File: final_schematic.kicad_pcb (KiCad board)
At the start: 2 copper layers, 47 parts, among them J1 Battery Babysitter, J2 BB_SYSOFF, J3 BOOT0, J4 OLED Qwiic, J5 Programmer, J8 GPS_COAX, SW1 SW_Push_SESS, SW2 SW_Push_RADIO, SW3 SW_Push_RST, U1 STM32L476VGTx, U2 MTK3339, U3 RFM95W-868S2, U4 BNO055, U5 LT1129-3.3_SO8

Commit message: pcb checkpoint
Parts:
- added REF**: MountingHole_2.1mm, MountingHole:MountingHole_2.1mm, F.Cu at (144.4, 67.7)
- added REF**: MountingHole_2.1mm, MountingHole:MountingHole_2.1mm, F.Cu at (116.5, 67.7)
- C10, C11, C14, C15, C16, C17, C2, C3, C4, C5, C6, C7, C8, C9: moved to B.Cu
- moved C8 97.0 mm to (138.0, 88.9), turned to 270 degrees
- moved C6 94.2 mm to (137.5, 79.7), turned to 270 degrees
- moved C10 87.6 mm to (134.8, 90.1), turned to 180 degrees
- moved R1 86.6 mm to (121.8, 68.0)
- moved C11 85.4 mm to (129.6, 90.1)
- moved D1 84.5 mm to (121.8, 64.3)
- moved C9 84.4 mm to (126.4, 88.5), turned to 90 degrees
- moved J3 75.6 mm to (116.8, 86.7), turned to 270 degrees
- moved R6 73.6 mm to (115.9, 89.1), turned to 180 degrees
- moved C4 72.8 mm to (115.0, 91.9), turned to 90 degrees
- moved C5 71.9 mm to (118.8, 91.3), turned to 90 degrees
- moved C7 60.9 mm to (127.5, 78.5)
- moved J5 55.3 mm to (120.5, 72.2), turned to 0 degrees
- moved U5 30.1 mm to (128.0, 106.0), turned to 270 degrees
- moved C12 29.5 mm to (126.1, 98.6), turned to 180 degrees
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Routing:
- net GND: track 0.00 -> 200.4 mm
- net 3V3: track 0.00 -> 127.2 mm, vias 0 -> 1
- net I2C1_SCL: track 0.00 -> 15.8 mm
- net I2C1_SDA: track 0.00 -> 14.6 mm
- net USART_TX: track 0.00 -> 12.6 mm
- net BOOT0: track 0.00 -> 10.7 mm
- net SWDIO: track 0.00 -> 9.47 mm
- net Net-(C2-Pad2): track 0.00 -> 7.06 mm
- net V_supply: track 0.00 -> 6.94 mm
- net Net-(C3-Pad2): track 0.00 -> 6.82 mm
- net SWCLK: track 0.00 -> 5.13 mm
- net Net-(LoRa_CON_Coaxial1-Pad1): track 0.00 -> 4.23 mm
- net Net-(J8-Pad1): track 0.00 -> 3.76 mm
- net IMU_nRST: track 0.00 -> 3.04 mm
- net DIO0: track 0.00 -> 2.85 mm
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
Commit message: PCB deconstruction
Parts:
- added REF**: MountingHole_2.1mm, MountingHole:MountingHole_2.1mm, F.Cu at (143.2, 97.8)
- added REF**: MountingHole_2.1mm, MountingHole:MountingHole_2.1mm, F.Cu at (116.6, 97.8)
- moved D1 3.41 mm to (120.2, 61.3)
- moved R1 3.41 mm to (120.2, 65.0)
- moved REF** 1.27 mm to (143.2, 67.7)
- moved C18 1.02 mm to (149.5, 77.0)
- moved U2 0.35 mm to (132.1, 64.4)
- moved REF** 0.05 mm to (116.6, 67.7)
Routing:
- net GND: track 200.4 -> 13.6 mm
- net I2C2_SCL: track 0.00 -> 31.9 mm
- net I2C2_SDA: track 0.00 -> 27.9 mm
- net 3V3: track 127.2 -> 109.2 mm
- net IMU_ADDR: track 0.00 -> 13.5 mm
- net USART_TX: track 12.6 -> 0.00 mm
- net IMU_INT: track 0.00 -> 11.7 mm
- net SWDIO: track 9.47 -> 0.00 mm
- net IMU_nRST: track 3.04 -> 12.1 mm
- net SWCLK: track 5.13 -> 0.00 mm
- net Net-(J8-Pad1): track 3.76 -> 0.00 mm

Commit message: latest and greatest
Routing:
- net I2C2_SDA: track 27.9 -> 39.0 mm
- net Net-(C1-Pad2): track 0.00 -> 5.58 mm
- net 3V3: track 109.2 -> 108.7 mm, vias 1 -> 0

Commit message: I think this is going well
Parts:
- removed REF** (x4): MountingHole_2.1mm, MountingHole:MountingHole_2.1mm
- added C19: .1uF, Capacitor_Tantalum_SMD:CP_EIA-3216-10_Kemet-I_Pad1.58x1.35mm_HandSolder, B.Cu at (121.3, 98.1)
- added D3: D_Zener, footprint_lib:1N5355BRLG, F.Cu at (22.9, 36.8)
- C1, C14, C2, C3: footprint Capacitor_SMD:C_0603_1608Metric_Pad1.08x0.95mm_HandSolder -> Capacitor_SMD:C_1206_3216Metric_Pad1.33x1.80mm_HandSolder
- C10, C11, C13, C18, C6, C7, C8, C9: footprint Capacitor_SMD:C_0402_1005Metric_Pad0.74x0.62mm_HandSolder -> Capacitor_SMD:C_0805_2012Metric_Pad1.18x1.45mm_HandSolder
- C15, C5: footprint Capacitor_SMD:C_0402_1005Metric_Pad0.74x0.62mm_HandSolder -> Capacitor_SMD:C_0805_2012Metric_Pad1.18x1.45mm_HandSolder; moved to F.Cu
- C16: footprint Capacitor_SMD:C_0603_1608Metric_Pad1.08x0.95mm_HandSolder -> Capacitor_SMD:C_2225_5664Metric_Pad1.80x6.60mm_HandSolder; moved to F.Cu
- C17: footprint Capacitor_SMD:C_0603_1608Metric_Pad1.08x0.95mm_HandSolder -> Capacitor_SMD:C_1210_3225Metric_Pad1.33x2.70mm_HandSolder; moved to F.Cu
- C4: footprint Capacitor_SMD:C_0603_1608Metric_Pad1.08x0.95mm_HandSolder -> Capacitor_SMD:C_1206_3216Metric_Pad1.33x1.80mm_HandSolder; moved to F.Cu
- D2: footprint Diode_SMD:D_0201_0603Metric_Pad0.64x0.40mm_HandSolder -> Diode_SMD:D_0603_1608Metric_Pad1.05x0.95mm_HandSolder
- R1, R10, R11, R2, R3, R4, R5, R6, R9: footprint Resistor_SMD:R_0603_1608Metric_Pad0.98x0.95mm_HandSolder -> Resistor_SMD:R_0805_2012Metric_Pad1.20x1.40mm_HandSolder
- Re1, Rf1: footprint Resistor_SMD:R_0603_1608Metric_Pad0.98x0.95mm_HandSolder -> Resistor_SMD:R_0815_2038Metric_Pad1.20x4.05mm_HandSolder
- moved J4 76.0 mm to (61.5, 29.0), turned to 0 degrees
- moved C5 64.1 mm to (55.1, 84.3), turned to 0 degrees
- moved C17 61.5 mm to (205.6, 58.8), turned to 0 degrees
- moved C15 59.3 mm to (205.6, 50.7), turned to 0 degrees
- moved J3 57.1 mm to (59.8, 84.2), turned to 0 degrees
- moved C18 57.1 mm to (205.5, 65.9), turned to 0 degrees
- moved C4 53.3 mm to (63.5, 77.9), turned to 0 degrees
- moved R1 52.1 mm to (79.5, 32.5), turned to 180 degrees
- moved R6 49.0 mm to (67.1, 84.0), turned to 0 degrees
- moved D1 47.7 mm to (79.5, 36.5), turned to 0 degrees
- moved C16 42.4 mm to (189.4, 62.0), turned to 0 degrees
- moved C13 39.4 mm to (127.9, 35.3)
- moved Re1 33.3 mm to (175.4, 62.2), turned to 180 degrees
- moved C1 33.0 mm to (113.1, 99.3), turned to 90 degrees
- moved Rf1 30.9 mm to (181.2, 61.6)
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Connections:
- U1 pad 1: session_btn -> Net-(U1-Pad1)
- U1 pad 12: Net-(U1-Pad12) -> BB_GPOUT
- U1 pad 13: Net-(U1-Pad13) -> BB_CE
- U1 pad 17: BB_CE -> Net-(U1-Pad17)
- U1 pad 18: BB_GPOUT -> Net-(U1-Pad18)
- U1 pad 2: radio_btn -> Net-(U1-Pad2)
- U1 pad 24: Net-(U1-Pad24) -> session_btn
- U1 pad 25: Net-(U1-Pad25) -> radio_btn
- U1 pad 26: Net-(U1-Pad26) -> LoRa_RST
- U1 pad 29: Net-(U1-Pad29) -> CS_LORA
- U1 pad 33: LoRa_RST -> Net-(U1-Pad33)
- U1 pad 34: CS_LORA -> Net-(U1-Pad34)
- U1 pad 44: BL_IND -> IMU_INT
- U1 pad 45: IMU_INT -> IMU_nRST
- U1 pad 46: IMU_nRST -> BL_IND
- U2 pad 9: N-00000104 -> USART_RX
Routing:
- net I2C2_SDA: track 39.0 -> 0.00 mm
- net (no net): track 0.00 -> 38.1 mm, vias 0 -> 4
- net I2C2_SCL: track 31.9 -> 0.00 mm
- net SYSOFF: track 2.76 -> 27.2 mm
- net radio_btn: track 0.00 -> 24.0 mm
- net I2C3_SDA: track 0.00 -> 20.0 mm
- net I2C3_SCL: track 0.00 -> 19.1 mm
- net BB_GPOUT: track 0.00 -> 17.9 mm
- net BB_CE: track 0.00 -> 16.7 mm
- net 3V3: track 108.7 -> 92.6 mm, vias 0 -> 2
- net I2C1_SCL: track 15.8 -> 0.00 mm
- net I2C1_SDA: track 14.6 -> 0.00 mm
- net GND: track 13.6 -> 0.00 mm
- net IMU_ADDR: track 13.5 -> 0.00 mm
- net Net-(C2-Pad2): track 7.06 -> 20.5 mm, vias 0 -> 1
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
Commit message: yep real well
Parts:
- C13, D3, Re1: moved to B.Cu
- moved D3 123.2 mm to (127.6, 101.8), turned to 180 degrees
- moved J4 73.9 mm to (116.0, 78.9), turned to 90 degrees
- moved C5 62.0 mm to (117.0, 88.6), turned to 90 degrees
- moved C18 58.4 mm to (147.3, 71.1), turned to 90 degrees
- moved C4 58.2 mm to (120.5, 89.2), turned to 90 degrees
- moved J3 57.2 mm to (117.0, 83.5), turned to 270 degrees
- moved C15 53.7 mm to (154.2, 66.2)
- moved R6 53.5 mm to (120.7, 84.5), turned to 270 degrees
- moved C17 52.1 mm to (153.6, 61.4), turned to 180 degrees
- moved D1 50.9 mm to (122.1, 64.3), turned to 270 degrees
- moved R1 50.8 mm to (122.1, 60.3), turned to 270 degrees
- moved C16 37.9 mm to (152.3, 54.1), turned to 180 degrees
- moved Re1 31.9 mm to (146.4, 75.4), turned to 0 degrees
- moved Rf1 31.6 mm to (149.9, 66.3)
- moved C13 28.8 mm to (126.4, 64.0)
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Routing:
- net 3V3: track 92.6 -> 181.4 mm, vias 2 -> 9
- net GND: track 0.00 -> 25.1 mm
- net I2C1_SCL: track 0.00 -> 14.9 mm
- net SWDIO: track 0.00 -> 13.9 mm
- net I2C1_SDA: track 0.00 -> 13.3 mm
- net USART_TX: track 0.00 -> 12.3 mm
- net USART_RX: track 0.00 -> 11.7 mm
- net BOOT0: track 0.00 -> 7.15 mm
- net Net-(J8-Pad1): track 0.00 -> 4.19 mm
- net Net-(D1-Pad1): track 0.00 -> 2.17 mm
- net SYSOFF: track 27.2 -> 27.7 mm

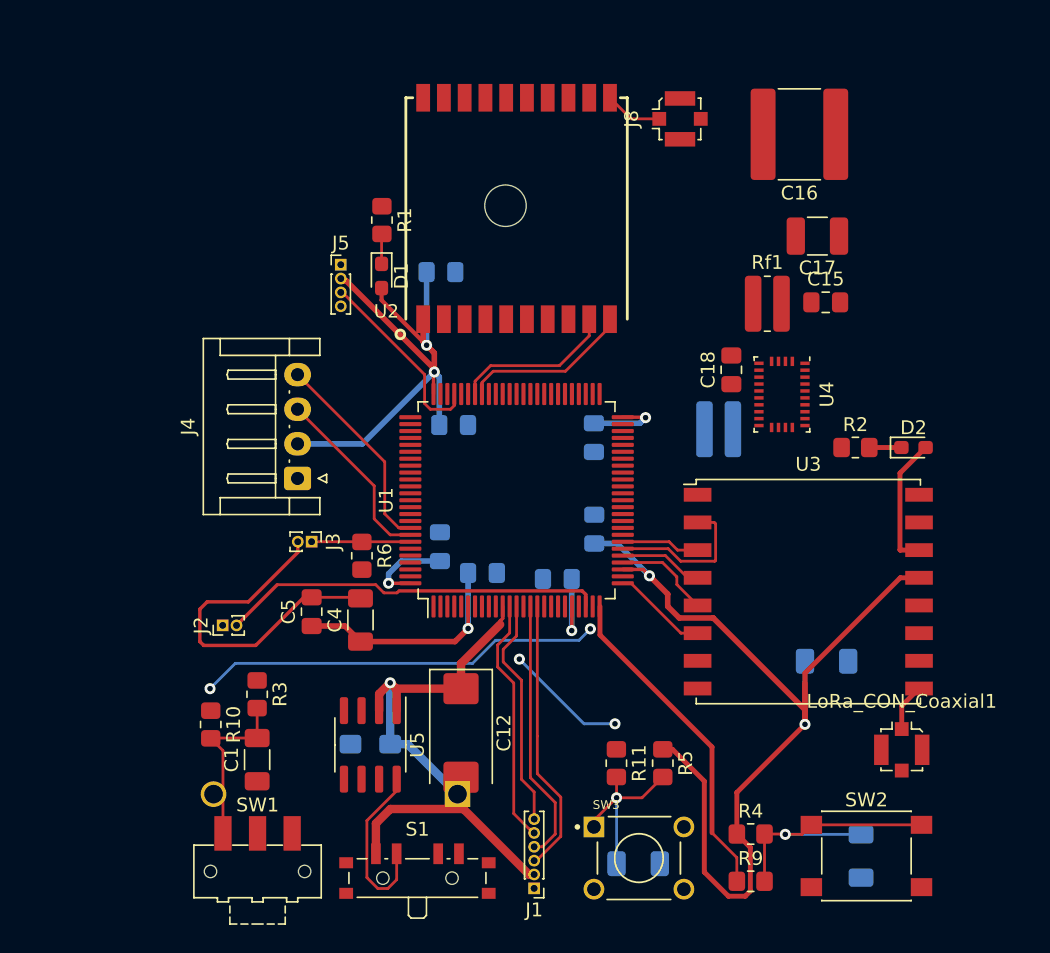
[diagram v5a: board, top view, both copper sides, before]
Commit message: Routing Complete
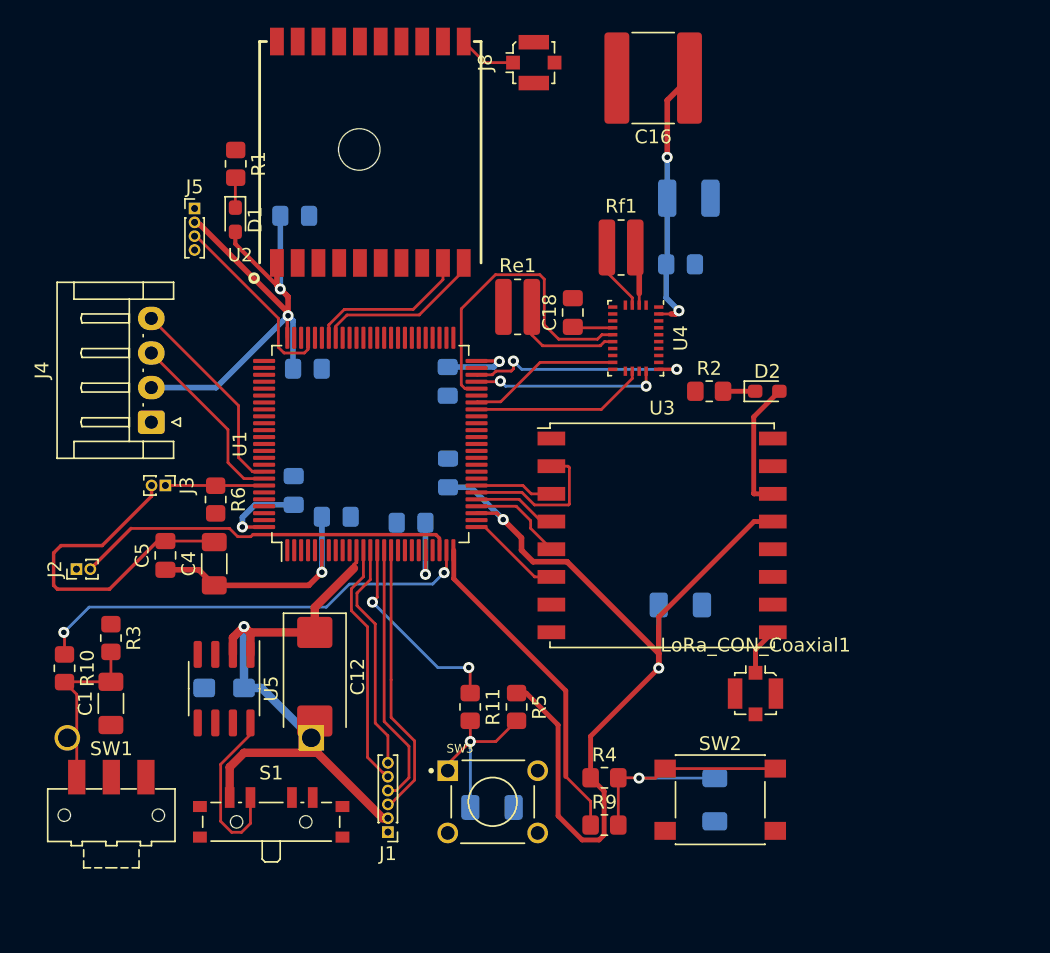
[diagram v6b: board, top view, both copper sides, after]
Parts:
- C15, C17: moved to B.Cu
- Re1: moved to F.Cu
- moved Re1 17.0 mm to (131.9, 66.5)
- moved C18 12.2 mm to (135.9, 67.0)
- moved C14 11.3 mm to (143.7, 88.1)
- moved R11 11.3 mm to (128.5, 95.5)
- moved R5 11.3 mm to (131.8, 95.5)
- moved SW2 11.3 mm to (146.5, 102.2)
- moved D2 11.3 mm to (149.9, 72.6)
- moved R4 11.3 mm to (138.2, 100.6)
- moved R9 11.3 mm to (138.2, 104.0)
- moved SW3 11.3 mm to (130.1, 102.3)
- moved C10 11.3 mm to (116.7, 71.0)
- moved C12 11.3 mm to (117.2, 93.3)
- moved C19 11.3 mm to (110.7, 94.1)
- moved C7 11.3 mm to (118.8, 81.7)
- moved C9 11.3 mm to (115.7, 79.8)
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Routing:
- net (no net): track 38.1 -> 0.00 mm, vias 4 -> 0
- net session_btn: track 0.00 -> 32.6 mm, vias 0 -> 2
- net 3V3: track 181.4 -> 205.5 mm, vias 9 -> 11
- net BL_IND: track 0.00 -> 22.7 mm
- net I2C2_SDA: track 0.00 -> 16.8 mm, vias 0 -> 2
- net NRST: track 0.00 -> 14.6 mm, vias 0 -> 2
- net I2C2_SCL: track 0.00 -> 13.5 mm, vias 0 -> 2
- net IMU_ADDR: track 0.00 -> 12.7 mm
- net IMU_INT: track 0.00 -> 11.0 mm
- net IMU_nRST: track 0.00 -> 8.32 mm
- net Net-(Rf1-Pad1): track 0.00 -> 4.92 mm
- net Net-(C18-Pad1): track 0.00 -> 2.91 mm

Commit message: Fill Added REVERT LOCATION
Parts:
- added REF**: MountingHole_2.1mm, MountingHole:MountingHole_2.1mm, F.Cu at (141.0, 96.0)
- added REF**: MountingHole_2.1mm, MountingHole:MountingHole_2.1mm, F.Cu at (149.0, 48.5)
- added REF**: MountingHole_2.1mm, MountingHole:MountingHole_2.1mm, F.Cu at (100.8, 48.5)
- moved D3 11.1 mm to (110.0, 89.0), turned to 0 degrees
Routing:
- net SWCLK: track 0.00 -> 10.2 mm
- net 3V3: track 205.5 -> 207.2 mm

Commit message: dimensions finalized
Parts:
- D1: value LED_HEARTBEAT_R1 -> HEART
- J5: value Programmer -> Prog
- REF** (x2): value MountingHole_2.1mm -> 2.1mm
- moved J5 1.23 mm to (107.4, 58.9)
- moved R6 1.05 mm to (109.1, 80.2)
- moved REF** 0.28 mm to (101.1, 48.5)
- moved S1 0.20 mm to (114.1, 103.6)
- moved SW1 0.10 mm to (102.5, 103.4)
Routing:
- net GND: track 25.1 -> 158.9 mm, vias 0 -> 21
- net 3V3: track 207.2 -> 201.1 mm
- net BB_Out: track 12.6 -> 7.89 mm, vias 0 -> 2
- net SWCLK: track 10.2 -> 11.5 mm
- net SWDIO: track 13.9 -> 15.0 mm
- added copper zone on B.Cu, net GND
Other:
- board outline added: 54.7 x 60.6 mm
